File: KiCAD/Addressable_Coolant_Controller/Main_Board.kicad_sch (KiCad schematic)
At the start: 1 part, among them U10 ProS3

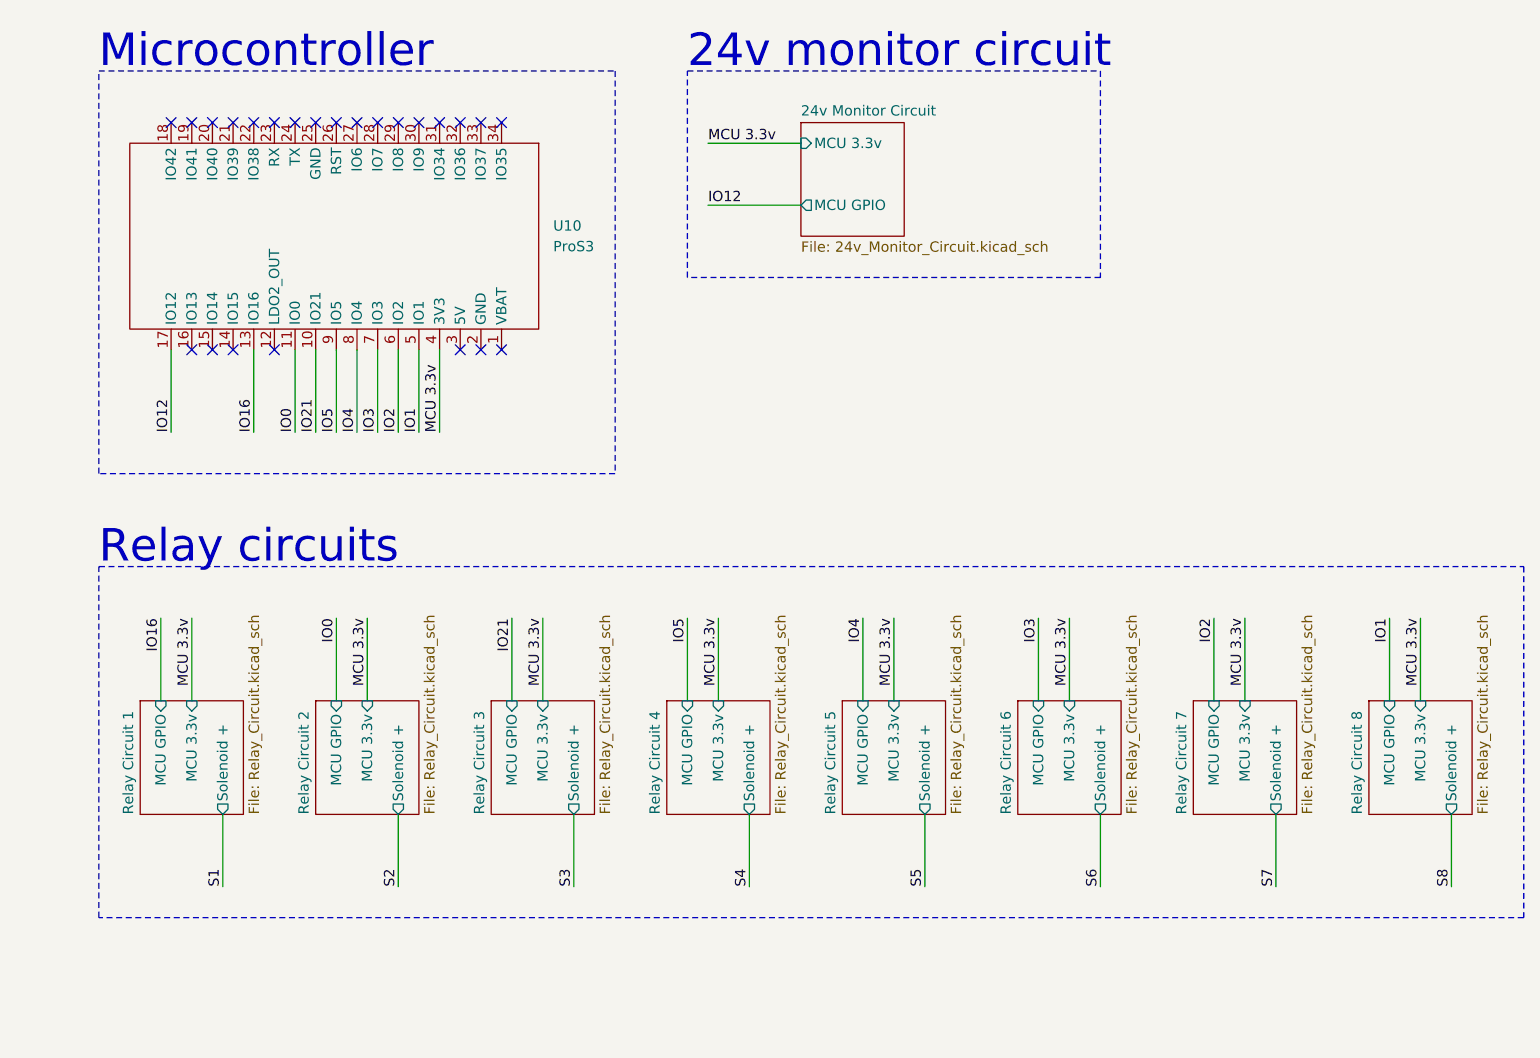
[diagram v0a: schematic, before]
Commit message: Updating KiCAD project to multi-board structure
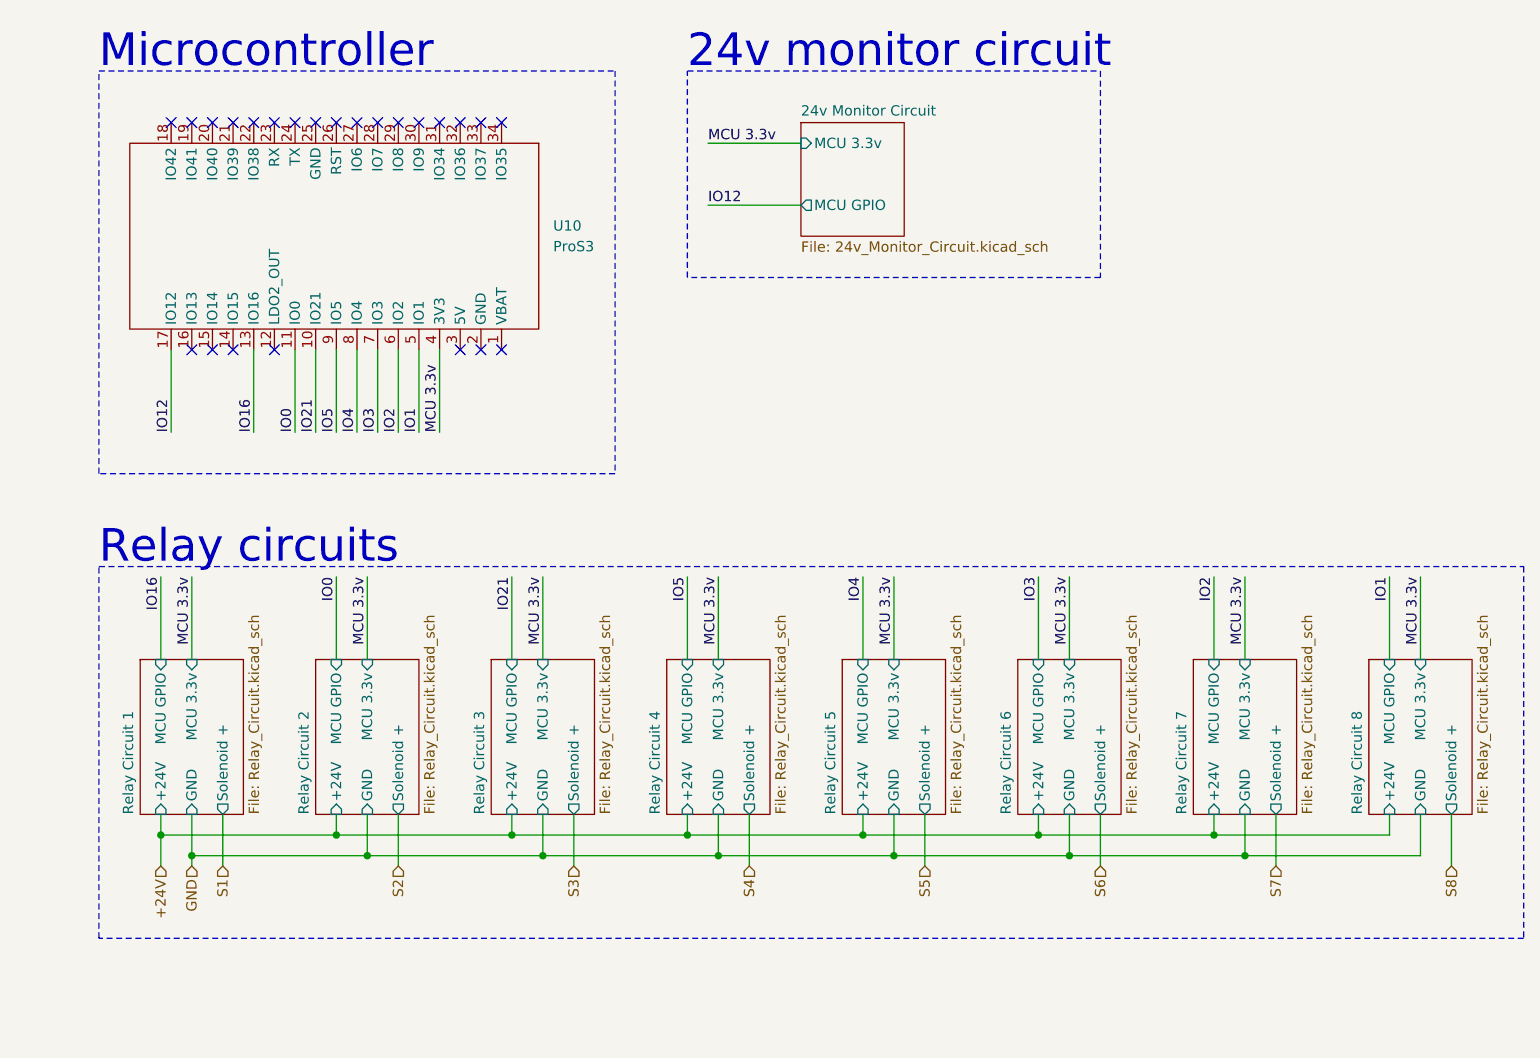
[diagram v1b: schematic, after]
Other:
- sheet Relay Circuit 1 ports: added +24V, GND; removed none
- sheet Relay Circuit 2 ports: added +24V, GND; removed none
- sheet Relay Circuit 3 ports: added +24V, GND; removed none
- sheet Relay Circuit 4 ports: added +24V, GND; removed none
- sheet Relay Circuit 5 ports: added +24V, GND; removed none
- sheet Relay Circuit 6 ports: added +24V, GND; removed none
- sheet Relay Circuit 7 ports: added +24V, GND; removed none
- sheet Relay Circuit 8 ports: added +24V, GND; removed none

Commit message: Added voltage divider and changed to 12 pin connectors
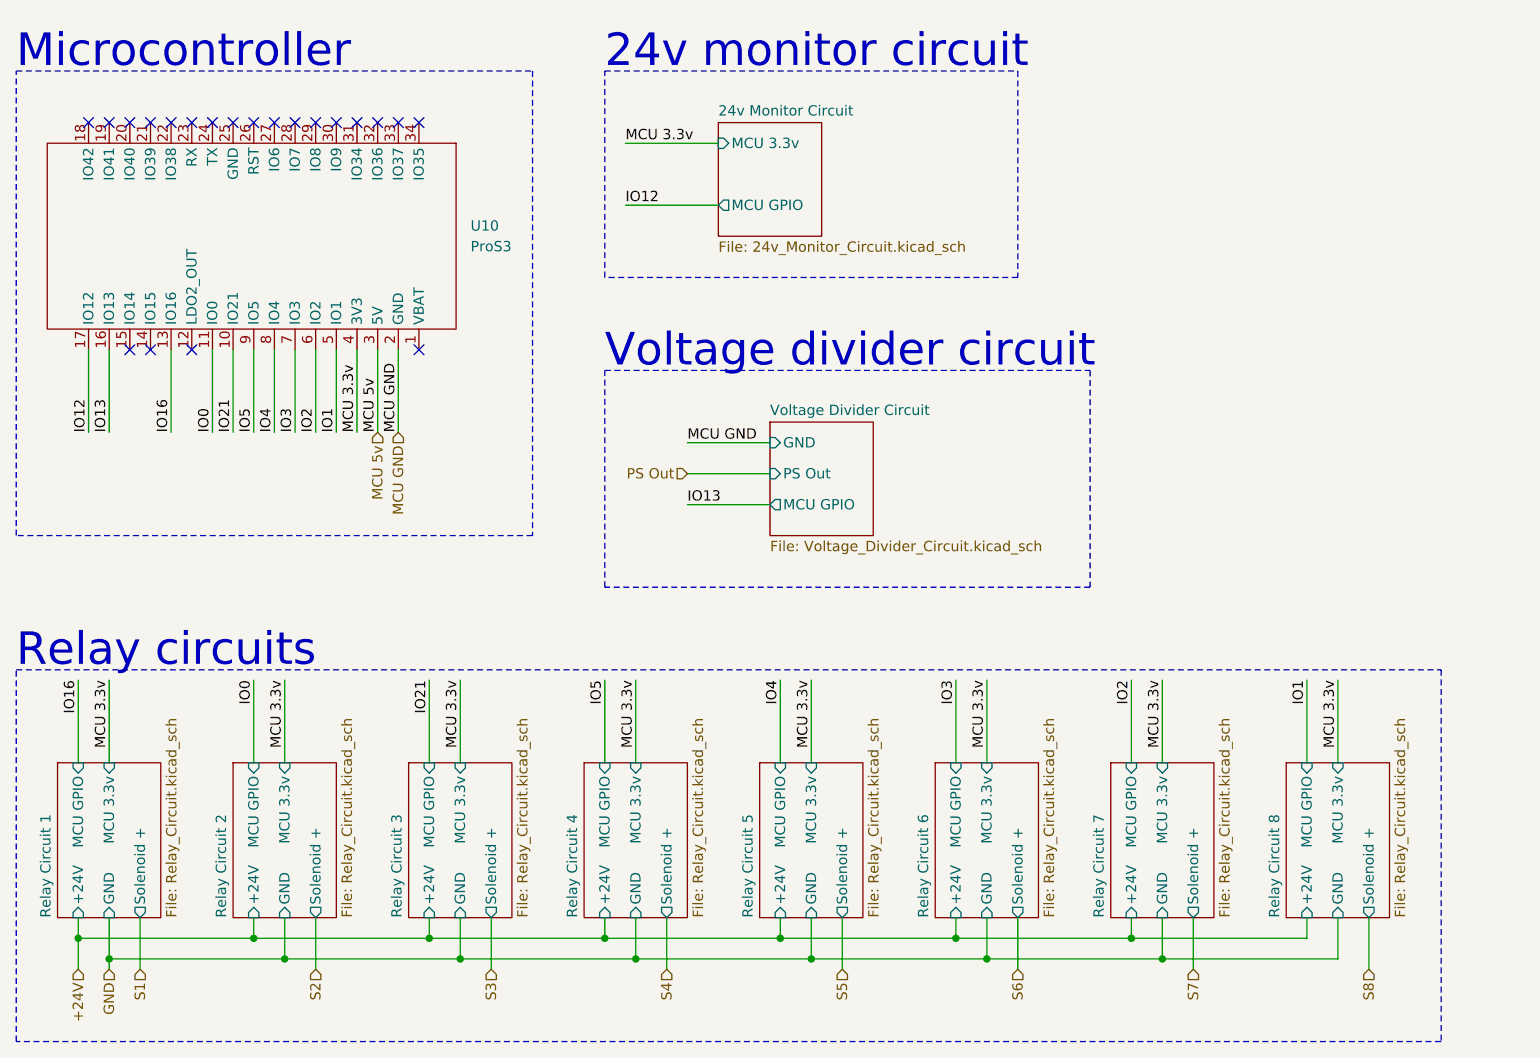
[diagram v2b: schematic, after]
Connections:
- net IO13: now reaches U10.16 (IO13)
- net MCU GND: now reaches U10.2 (GND)
- net MCU 5v: now reaches U10.3 (5V)
- no-connect marks 24 -> 21
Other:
- added sheet Voltage Divider Circuit (Voltage_Divider_Circuit.kicad_sch)
- note added: "Voltage divider circuit"
- moved on the sheet: U10

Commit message: Fixed broken netclasses, removed voltage divider circuit
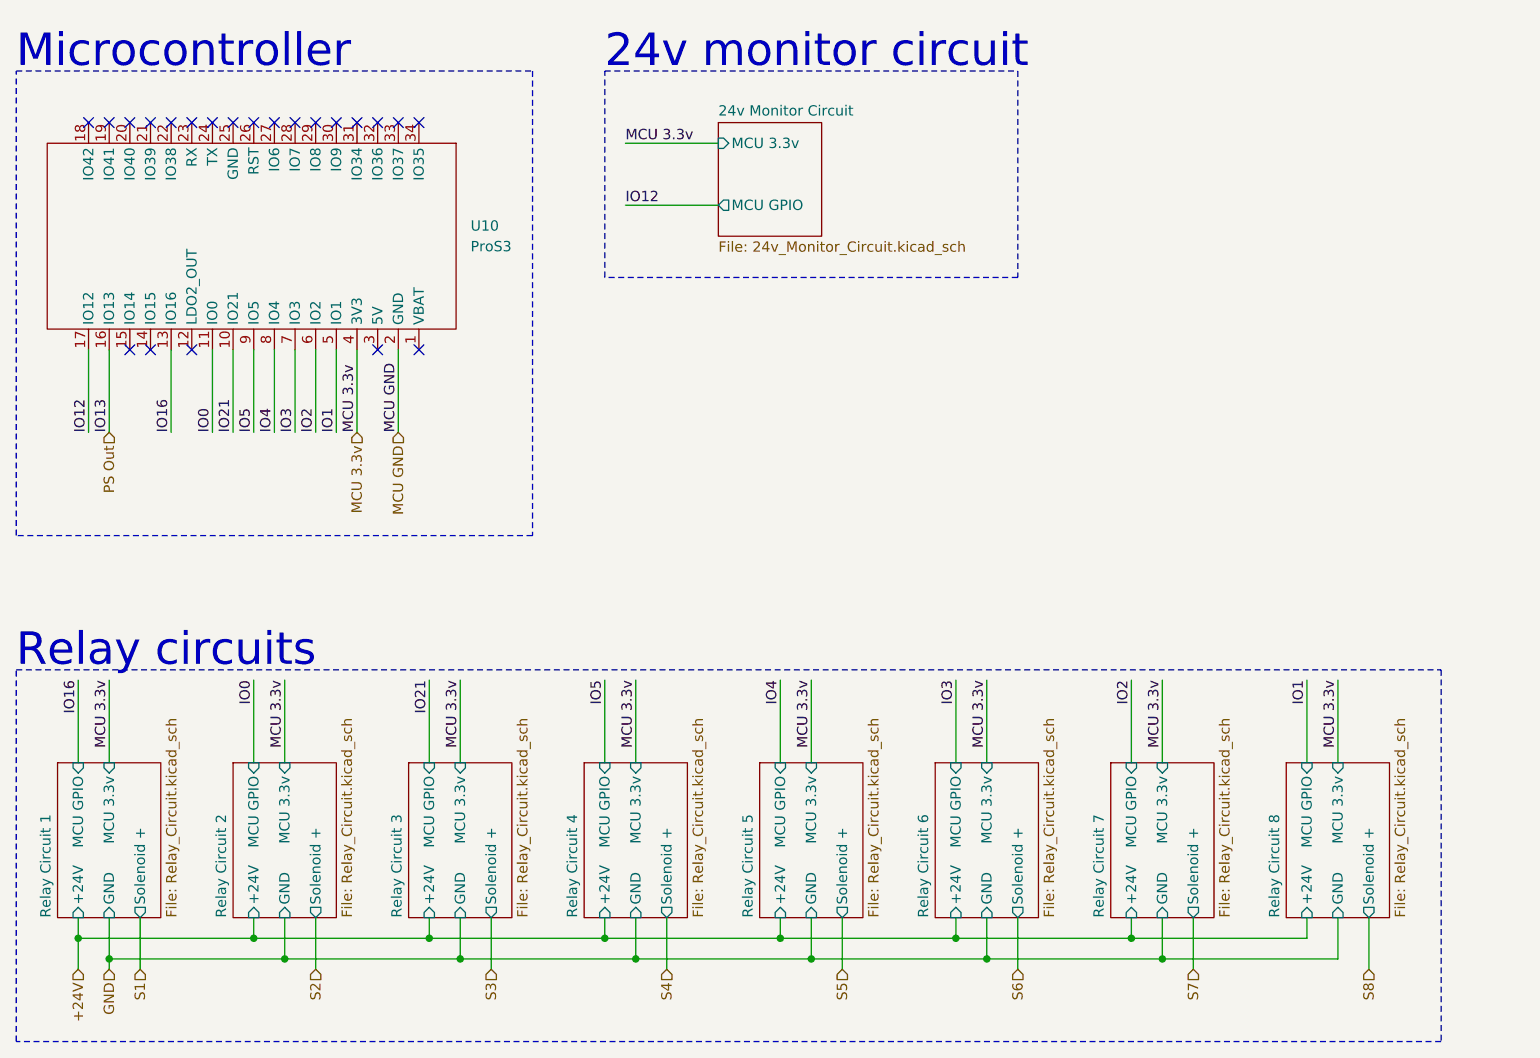
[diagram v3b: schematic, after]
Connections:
- net IO13 is gone; now on net PS Out: U10.16 (IO13)
- net MCU 5v: no longer names the net of U10.3 (5V)
- no-connect marks 21 -> 22
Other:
- removed sheet Voltage Divider Circuit
- note removed: "Voltage divider circuit"
- company: (none) -> Warner Consulting Inc.
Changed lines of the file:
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@@
 (kicad_sch (version 20230121) (generator eeschema)
   (paper "A4")
+  (title_block
+    (company "Warner Consulting Inc.")
+  )
   (junction (at 161.29 132.08) (diameter 0) (color 0 0 0 0)
   )
@@
   (no_connect (at 39.37 29.21))
   (no_connect (at 41.91 57.15))
+  (no_connect (at 64.77 57.15))
   (no_connect (at 36.83 57.15))
   (no_connect (at 44.45 29.21))
@@
   (no_connect (at 36.83 29.21))
   (no_connect (at 52.07 29.21))
-  (wire (pts (xy 102.87 76.2) (xy 113.03 76.2))
-    (stroke (width 0) (type default))
-  )
   (wire (pts (xy 31.75 127) (xy 31.75 132.08))
     (stroke (width 0) (type default))
@@
     (stroke (width 0) (type default))
   )
-  (wire (pts (xy 102.87 68.58) (xy 113.03 68.58))
-    (stroke (width 0) (type default))
-  )
   (wire (pts (xy 78.74 127) (xy 78.74 133.35))
     (stroke (width 0) (type default))
@@
     (stroke (width 0) (type default))
   )
-  (wire (pts (xy 64.77 57.15) (xy 64.77 67.31))
-    (stroke (width 0) (type default))
-  )
   (wire (pts (xy 135.89 97.79) (xy 135.89 107.95))
     (stroke (width 0) (type default))
@@
   )
   (wire (pts (xy 31.75 132.08) (xy 53.34 132.08))
-    (stroke (width 0) (type default))
-  )
-  (wire (pts (xy 102.87 72.39) (xy 113.03 72.39))
     (stroke (width 0) (type default))
   )
@@
     (fill (type none))
   )
-  (rectangle (start 92.71 59.69) (end 152.4 86.36)
-    (stroke (width 0) (type dash_dot_dot))
-    (fill (type none))
-  )
   (text "Microcontroller" (at 20.32 22.86 0)
     (effects (font (size 4 4)) (justify left bottom))
@@
     (effects (font (size 4 4)) (justify left bottom))
   )
-  (text "Voltage divider circuit" (at 92.71 59.69 0)
-    (effects (font (size 4 4)) (justify left bottom))
-  )
-  (label "MCU GND" (at 102.87 68.58 0) (fields_autoplaced)
-    (effects (font (size 1.27 1.27)) (justify left bottom))
-  )
   (label "IO12" (at 29.21 67.31 90) (fields_autoplaced)
     (effects (font (size 1.27 1.27)) (justify left bottom))
@@
     (effects (font (size 1.27 1.27)) (justify left bottom))
   )
-  (label "IO13" (at 102.87 76.2 0) (fields_autoplaced)
-    (effects (font (size 1.27 1.27)) (justify left bottom))
-  )
   (label "MCU 3.3v" (at 53.34 97.79 270) (fields_autoplaced)
     (effects (font (size 1.27 1.27)) (justify right bottom))
@@
     (effects (font (size 1.27 1.27)) (justify left bottom))
   )
-  (label "MCU 5v" (at 64.77 67.31 90) (fields_autoplaced)
-    (effects (font (size 1.27 1.27)) (justify left bottom))
-  )
   (label "MCU 3.3v" (at 31.75 97.79 270) (fields_autoplaced)
     (effects (font (size 1.27 1.27)) (justify right bottom))
@@
     (effects (font (size 1.27 1.27)) (justify left bottom))
   )
+  (hierarchical_label "MCU 3.3v" (shape input) (at 62.23 67.31 270) (fields_autoplaced)
+    (effects (font (size 1.27 1.27)) (justify right))
+  )
   (hierarchical_label "S2" (shape input) (at 57.15 133.35 270) (fields_autoplaced)
     (effects (font (size 1.27 1.27)) (justify right))
@@
     (effects (font (size 1.27 1.27)) (justify right))
   )
+  (hierarchical_label "PS Out" (shape input) (at 31.75 67.31 270) (fields_autoplaced)
+    (effects (font (size 1.27 1.27)) (justify right))
+  )
   (hierarchical_label "MCU GND" (shape input) (at 67.31 67.31 270) (fields_autoplaced)
     (effects (font (size 1.27 1.27)) (justify right))
   )
   (hierarchical_label "S1" (shape input) (at 35.56 133.35 270) (fields_autoplaced)
-    (effects (font (size 1.27 1.27)) (justify right))
-  )
-  (hierarchical_label "MCU 5v" (shape input) (at 64.77 67.31 270) (fields_autoplaced)
-    (effects (font (size 1.27 1.27)) (justify right))
-  )
-  (hierarchical_label "PS Out" (shape input) (at 102.87 72.39 180) (fields_autoplaced)
     (effects (font (size 1.27 1.27)) (justify right))
   )
@@
       )
     )
-  )
-  (sheet (at 113.03 66.04) (size 12.7 13.97) (fields_autoplaced)
-    (stroke (width 0.1524) (type solid))
-    (fill (color 0 0 0 0.0000))
-    (property "Sheetname" "Voltage Divider Circuit" (at 113.03 65.3284 0)
-      (effects (font (size 1.27 1.27)) (justify left bottom))
-    )
-    (property "Sheetfile" "Voltage_Divider_Circuit.kicad_sch" (at 113.03 80.5946 0)
-      (effects (font (size 1.27 1.27)) (justify left top))
-    )
-    (pin "GND" input (at 113.03 68.58 180)
-      (effects (font (size 1.27 1.27)) (justify left))
-    )
-    (pin "PS Out" input (at 113.03 72.39 180)
-      (effects (font (size 1.27 1.27)) (justify left))
-    )
-    (pin "MCU GPIO" output (at 113.03 76.2 180)
-      (effects (font (size 1.27 1.27)) (justify left))
-    )
-    (instances
-      (project "Addressable_Coolant_Controller"
-        (path "/603d0a2e-fca7-40af-8fa8-51b59d823d4d/9e308de8-a8a3-4754-85bb-a6ac18661119" (page "13"))
-      )
-    )
